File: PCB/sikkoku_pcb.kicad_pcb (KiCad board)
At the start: 2 copper layers, 290 x 153 mm, 25 parts, among them J1 Conn_01x03, SW1 SW_PUSH, SW10 SW_PUSH, SW11 SW_PUSH, SW12 SW_PUSH, SW13 SW_PUSH, SW14 SW_PUSH, SW15 SW_PUSH, SW16 SW_PUSH, SW17 SW_PUSH, SW2 SW_PUSH, SW3 SW_PUSH, SW4 SW_PUSH, SW5 SW_PUSH, SW6 SW_PUSH, SW7 SW_PUSH, SW8 SW_PUSH, SW9 SW_PUSH

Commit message: 配線が完了 DRC済
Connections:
- SW1 pad 2: Net-(A1-GPIO2) -> Net-(A1-GPIO3)
- SW10 pad 2: Net-(A1-GPIO11) -> Net-(A1-GPIO8)
- SW11 pad 2: Net-(A1-GPIO12) -> Net-(A1-GPIO9)
- SW12 pad 2: Net-(A1-GPIO13) -> Net-(A1-GPIO10)
- SW13 pad 2: Net-(A1-GPIO14) -> Net-(A1-GPIO11)
- SW14 pad 2: Net-(A1-GPIO15) -> Net-(A1-GPIO7)
- SW2 pad 2: Net-(A1-GPIO3) -> Net-(A1-GPIO4)
- SW3 pad 2: Net-(A1-GPIO4) -> Net-(A1-GPIO5)
- SW4 pad 2: Net-(A1-GPIO5) -> Net-(A1-GPIO6)
- SW5 pad 2: Net-(A1-GPIO6) -> Net-(A1-GPIO2)
- SW6 pad 2: Net-(A1-GPIO7) -> Net-(A1-GPIO12)
- SW7 pad 2: Net-(A1-GPIO8) -> Net-(A1-GPIO13)
- SW8 pad 2: Net-(A1-GPIO9) -> Net-(A1-GPIO14)
- SW9 pad 2: Net-(A1-GPIO10) -> Net-(A1-GPIO15)
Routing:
- net GND: track 0.00 -> 912.2 mm, vias 0 -> 24
- net Net-(A1-GPIO11): track 0.00 -> 221.3 mm
- net Net-(A1-GPIO10): track 0.00 -> 205.5 mm
- net Net-(A1-GPIO15): track 0.00 -> 193.7 mm
- net Net-(A1-GPIO9): track 0.00 -> 190.0 mm
- net Net-(A1-GPIO7): track 0.00 -> 188.4 mm
- net Net-(A1-GPIO14): track 0.00 -> 176.7 mm
- net Net-(A1-GPIO8): track 0.00 -> 176.2 mm
- net Net-(A1-GPIO13): track 0.00 -> 165.4 mm
- net Net-(A1-GPIO12): track 0.00 -> 151.7 mm
- net Net-(A1-GPIO16): track 0.00 -> 150.9 mm
- net Net-(A1-GPIO2): track 0.00 -> 149.4 mm
- net Net-(A1-GPIO17): track 0.00 -> 135.3 mm
- net Net-(A1-GPIO6): track 0.00 -> 105.3 mm
- net Net-(A1-GPIO5): track 0.00 -> 90.7 mm
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- added copper zone on B.Cu, net GND
- added copper zone on F.Cu, net GND

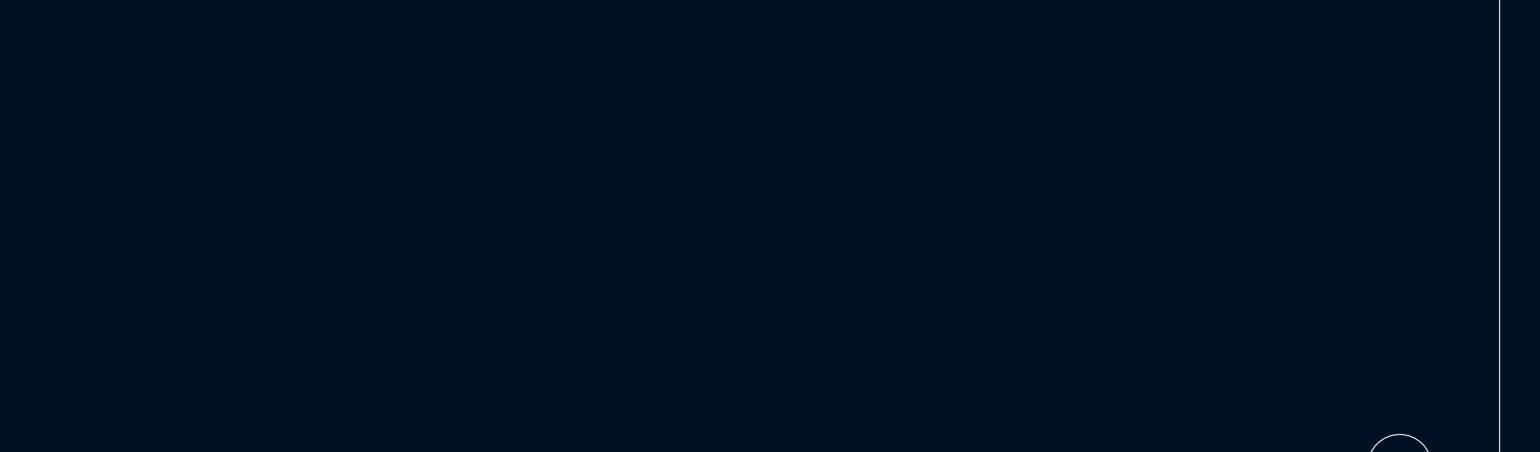
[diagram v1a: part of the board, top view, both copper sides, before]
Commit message: 名前とかのシルクを追加
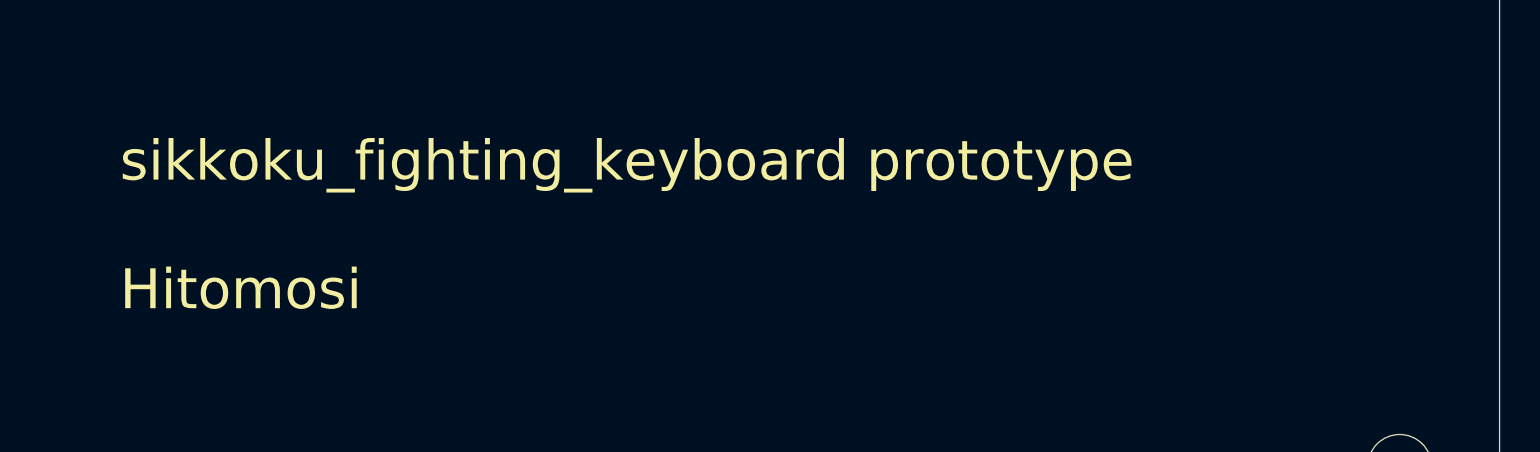
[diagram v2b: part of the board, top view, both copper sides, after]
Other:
- board text added: "sikkoku_fighting_keyboard prototype Hitomosi"
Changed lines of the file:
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@@
 		(layer "Edge.Cuts")
+	)
+	(gr_text "sikkoku_fighting_keyboard prototype\n\nHitomosi"
+		(at 215.9 147.32 0)
+		(layer "F.SilkS")
+		(effects
+			(font
+				(size 2 2)
+				(thickness 0.25)
+			)
+			(justify left bottom)
+		)
 	)
 	(dimension
@@
 		(layer "Cmts.User")
 		(pts
+			(xy 140 155) (xy 0 156.21)
+		)
+		(height 13.91)
+		(orientation 0)
+		(format
+			(prefix "")
+			(suffix "")
+			(units 3)
+			(units_format 0)
+			(precision 4)
+			(suppress_zeroes yes)
+		)
+		(style
+			(thickness 0.1)
+			(arrow_length 1.27)
+			(text_position_mode 0)
+			(arrow_direction outward)
+			(extension_height 0.58642)
+			(extension_offset 0.5)
+			(keep_text_aligned yes)
+		)
+		(gr_text "140"
+			(at 70 167.76 0)
+			(layer "Cmts.User")
+			(effects
+				(font
+					(size 1 1)
+					(thickness 0.15)
+				)
+			)
+		)
+	)
+	(dimension
+		(type orthogonal)
+		(layer "Cmts.User")
+		(pts
 			(xy 235.057772 55.247314) (xy 285 55.247314)
 		)
@@
 		)
 	)
+	(dimension
+		(type orthogonal)
+		(layer "Cmts.User")
+		(pts
+			(xy 140 155) (xy 280 155)
+		)
+		(height 13.91)
+		(orientation 0)
+		(format
+			(prefix "")
+			(suffix "")
+			(units 3)
+			(units_format 0)
+			(precision 4)
+			(suppress_zeroes yes)
+		)
+		(style
+			(thickness 0.1)
+			(arrow_length 1.27)
+			(text_position_mode 0)
+			(arrow_direction outward)
+			(extension_height 0.58642)
+			(extension_offset 0.5)
+			(keep_text_aligned yes)
+		)
+		(gr_text "140"
+			(at 210 167.76 0)
+			(layer "Cmts.User")
+			(effects
+				(font
+					(size 1 1)
+					(thickness 0.15)
+				)
+			)
+		)
+	)
 	(segment
 		(start 186.69 58.42)
@@
 				(xy 22.86 24.13) (xy 43.18 24.13) (xy 43.18 27.94) (xy 44.45 29.21) (xy 44.45 31.75) (xy 43.18 33.02)
 				(xy 43.18 36.83) (xy 12.7 36.83) (xy 12.7 33.02) (xy 11.43 31.75) (xy 6.985 31.75) (xy 2.54 31.75)
-				(xy 2.54 24.13) (xy 8.89 24.13) (xy 8.89 24.13) (xy 16.51 31.75) (xy 19.05 31.75) (xy 22.86 27.94)
+				(xy 2.54 24.13) (xy 8.89 24.13) (xy 16.51 31.75) (xy 19.05 31.75) (xy 22.86 27.94)
 			)
 		)

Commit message: gerber_to_orderを用いてガーバーデータ作成 発注
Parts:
- moved REF** 19.1 mm to (158.1, 18.2)
- moved REF** 19.1 mm to (298.1, 18.2)
- moved SW10 19.1 mm to (198.1, 76.2)
- moved SW11 19.1 mm to (216.5, 71.3)
- moved SW13 19.1 mm to (253.2, 61.4)
- moved SW15 19.1 mm to (186.1, 28.2)
- moved SW16 19.1 mm to (205.1, 28.2)
- moved SW8 19.1 mm to (230.2, 49.0)
- moved REF** 19.1 mm to (298.1, 161.2)
- moved REF** 19.1 mm to (158.1, 161.2)
- moved SW2 19.1 mm to (81.4, 66.4)
- moved A1 19.1 mm to (40.2, 36.9)
- moved SW1 19.1 mm to (49.7, 76.5)
- moved SW3 19.1 mm to (99.8, 71.3)
- moved SW4 19.1 mm to (118.1, 76.2)
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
